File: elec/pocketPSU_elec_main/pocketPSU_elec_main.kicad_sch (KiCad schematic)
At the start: 0 parts

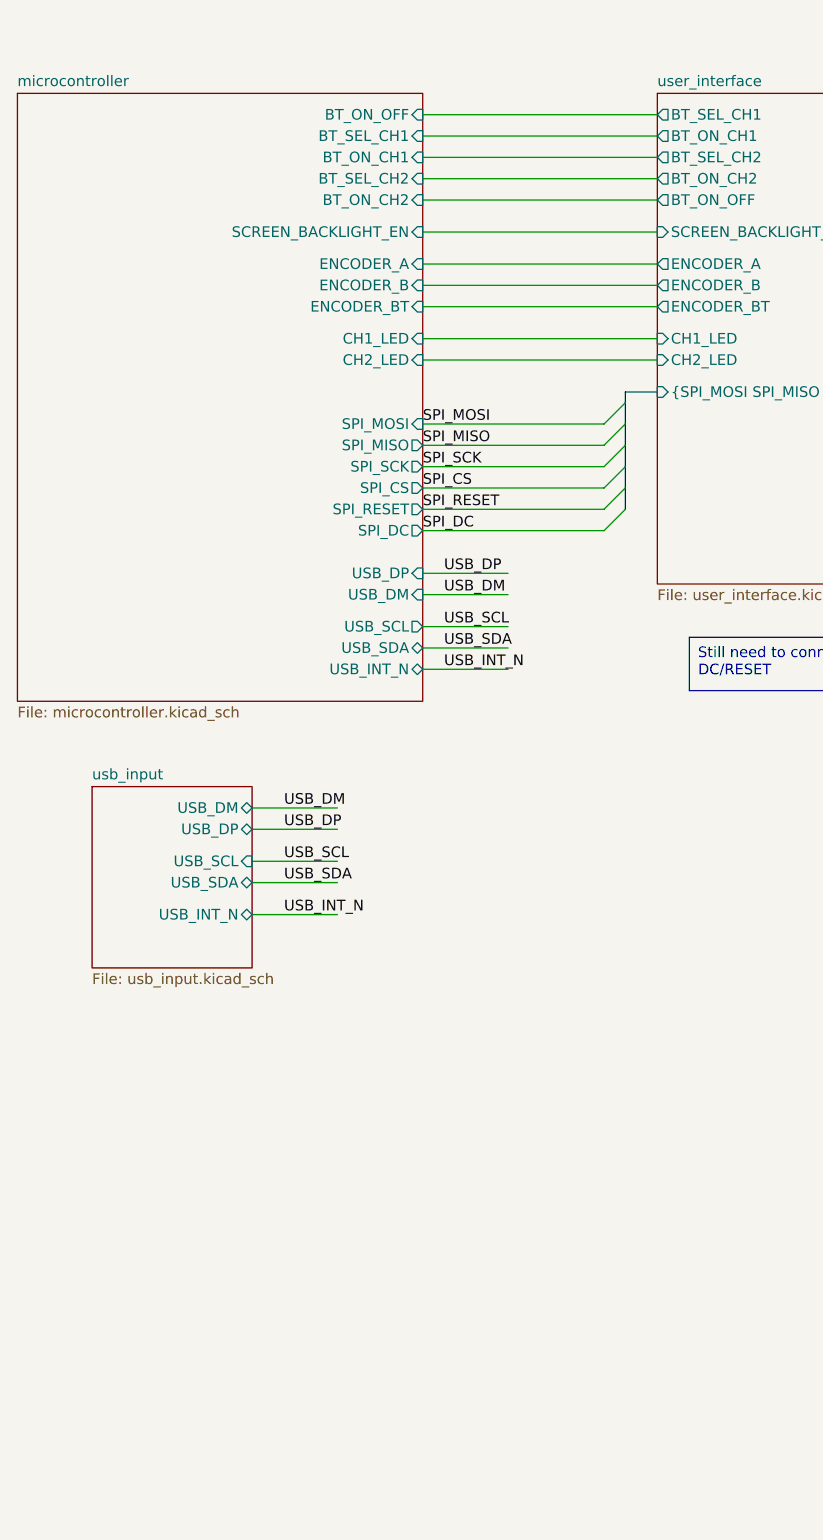
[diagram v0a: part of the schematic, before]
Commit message: move components, add mounting holes
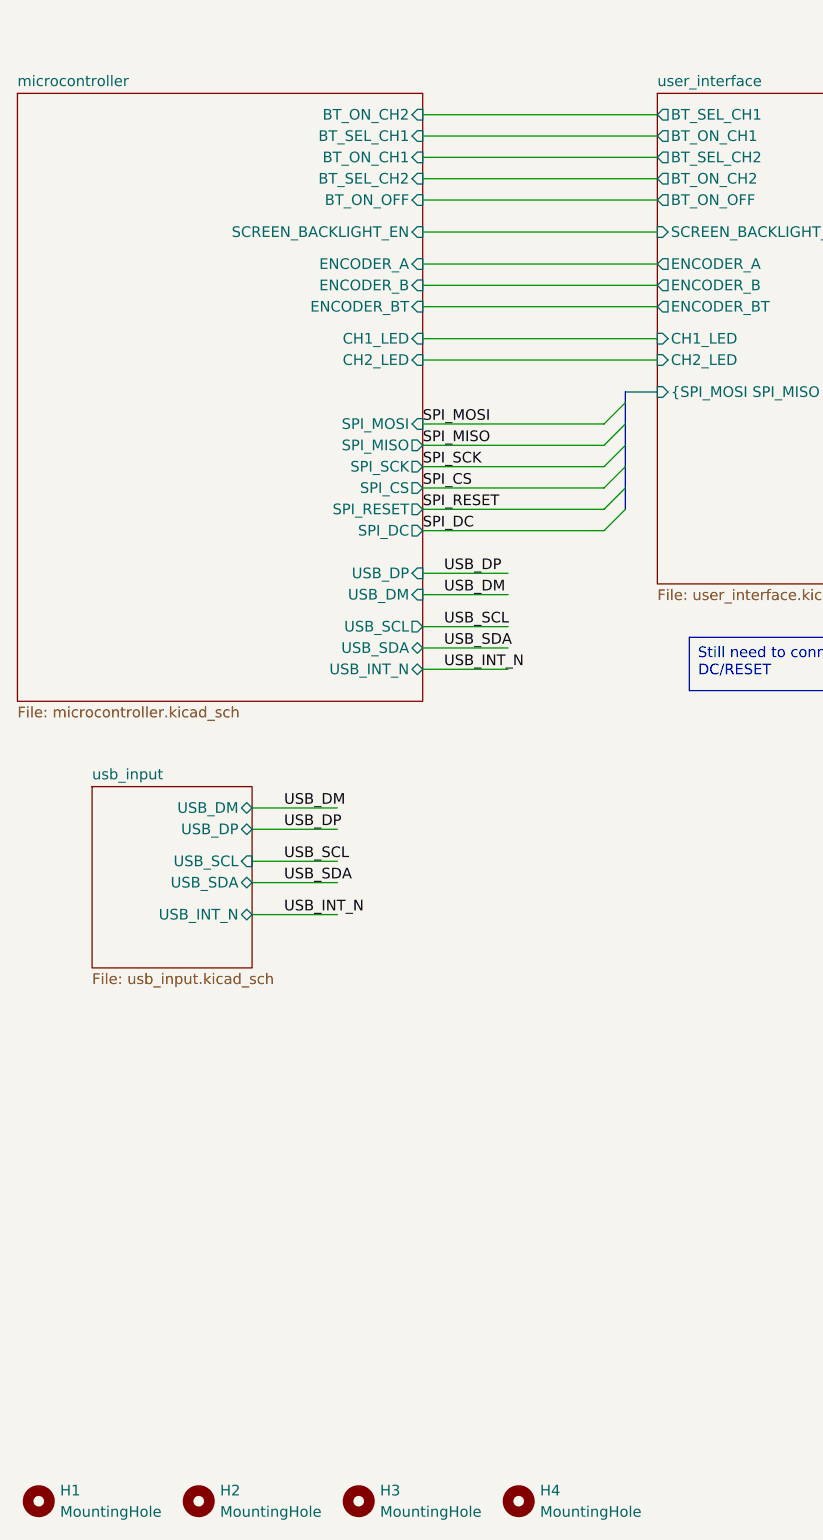
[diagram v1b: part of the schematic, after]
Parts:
- added H1, H2, H3, H4: MountingHole, MountingHole:MountingHole_3.7mm_Pad_Via, symbol Mechanical:MountingHole
